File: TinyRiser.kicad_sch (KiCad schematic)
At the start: 25 parts, among them J2 Bus_PCI_Express_x16, J3 Bus_M.2_Socket_M, J5 Conn_02x04_Odd_Even, M1 Fan_4pin

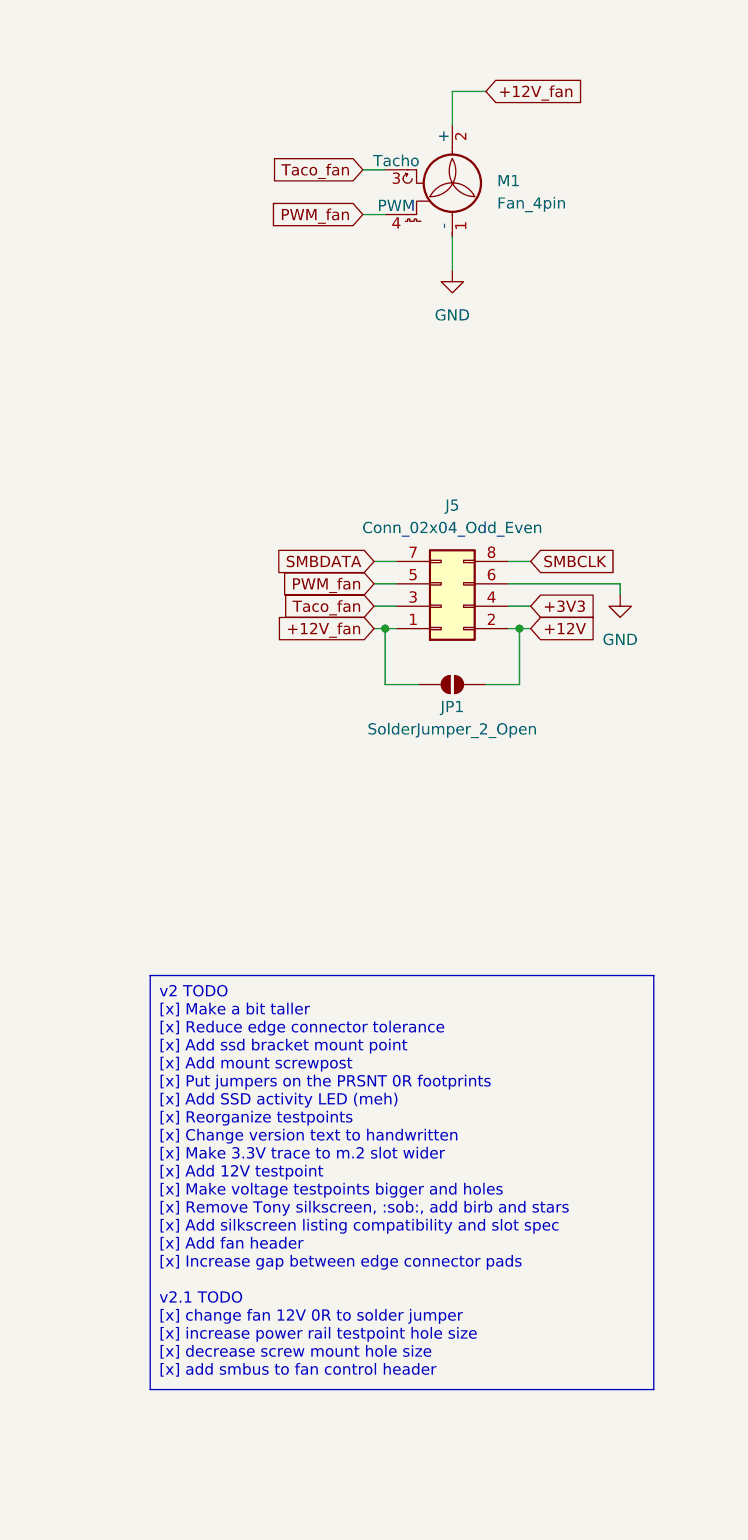
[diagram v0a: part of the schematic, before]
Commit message: Added JLC Assembly files and complete part list
Files exported using JLCPCB Tools 2026.04.03, not tested, please verify order on checkout.

Also updated PCB file from KiCad 8 to KiCad 9
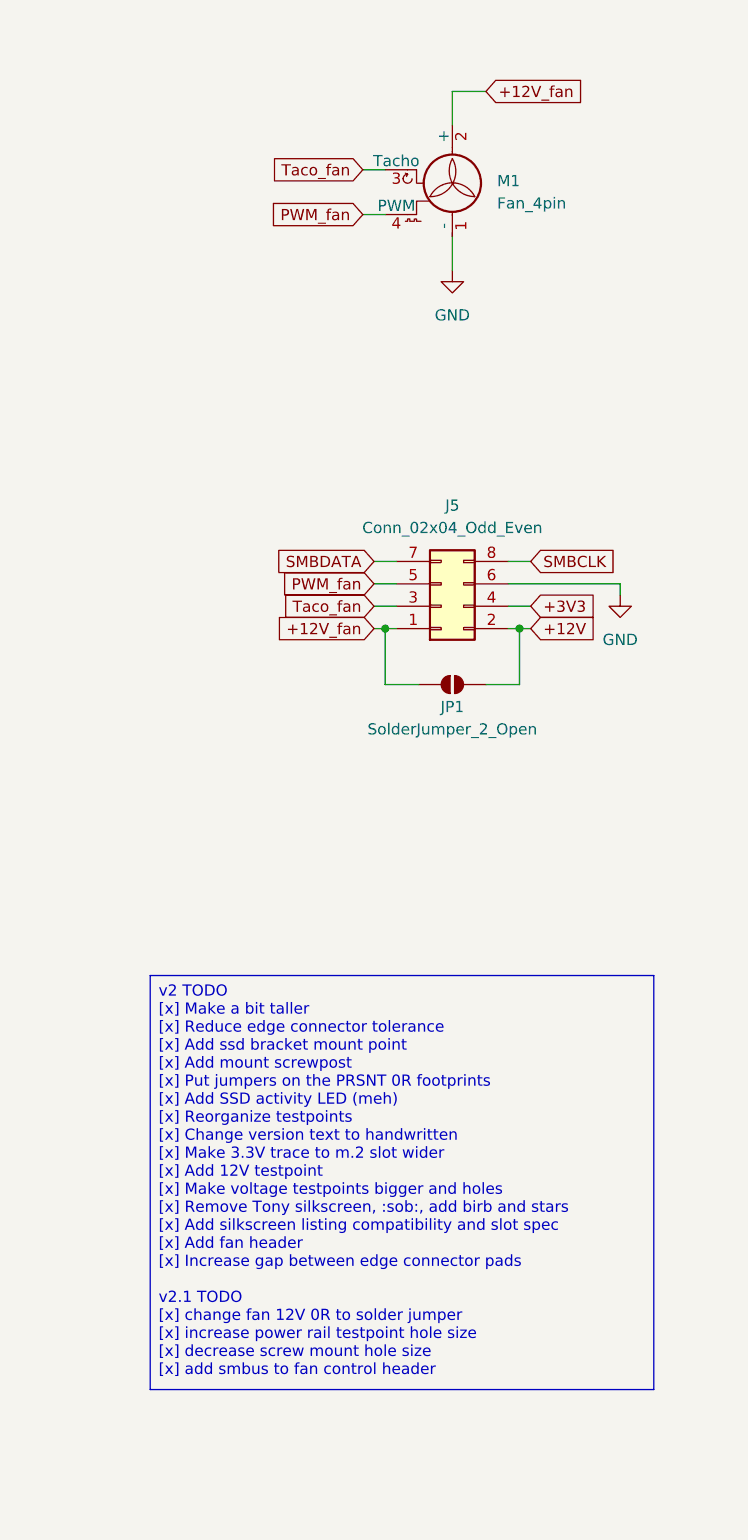
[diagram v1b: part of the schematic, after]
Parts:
- H1: LCSC Part (none) -> C5301786
- J1, J5, M1, R3, R4, R5, R6, TP1, TP2, TP3, TP4, TP5, TP6, TP7, TP8, TP9: now left out of the parts list
- J2: LCSC Part (none) -> C404116
- J3: LCSC Part (none) -> C41430861
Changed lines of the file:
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@@
 (kicad_sch
-	(version 20231120)
+	(version 20250114)
 	(generator "eeschema")
-	(generator_version "8.0")
+	(generator_version "9.0")
 	(paper "A3")
 	(title_block
@@
 		(comment 4 "nya")
 	)
+	(rectangle
+		(start 186.69 255.27)
+		(end 223.52 269.24)
+		(stroke
+			(width 0)
+			(type default)
+		)
+		(fill
+			(type none)
+		)
+	)
+	(text "Not a typo, that's how it's\nspelled on Lenovo's schematic"
+		(exclude_from_sim no)
+		(at 191.77 267.97 0)
+		(effects
+			(font
+				(size 1.27 1.27)
+			)
+			(justify left bottom)
+		)
+	)
+	(text "Note: CLKREQ# needs to be connected to GND to activate the clock signal.\nIf you're replacing the PCIe slot with an open-ended one,\nmake sure to account for longer cards where the presence pin is outside the slot.\nMaybe just hard-wire CLKREQ# to GND"
+		(exclude_from_sim no)
+		(at 237.744 22.606 0)
+		(effects
+			(font
+				(size 1.27 1.27)
+			)
+			(justify left)
+		)
+	)
+	(text_box "v2 TODO\n[x] Make a bit taller\n[x] Reduce edge connector tolerance\n[x] Add ssd bracket mount point\n[x] Add mount screwpost\n[x] Put jumpers on the PRSNT 0R footprints\n[x] Add SSD activity LED (meh)\n[x] Reorganize testpoints\n[x] Change version text to handwritten\n[x] Make 3.3V trace to m.2 slot wider\n[x] Add 12V testpoint\n[x] Make voltage testpoints bigger and holes\n[x] Remove Tony silkscreen, :sob:, add birb and stars\n[x] Add silkscreen listing compatibility and slot spec\n[x] Add fan header\n[x] Increase gap between edge connector pads\n\nv2.1 TODO\n[x] change fan 12V 0R to solder jumper\n[x] increase power rail testpoint hole size\n[x] decrease screw mount hole size\n[x] add smbus to fan control header"
+		(exclude_from_sim no)
+		(at 345.44 189.23 0)
+		(size 57.15 46.99)
+		(margins 0.9525 0.9525 0.9525 0.9525)
+		(stroke
+			(width 0)
+			(type default)
+		)
+		(fill
+			(type none)
+		)
+		(effects
+			(font
+				(size 1.27 1.27)
+			)
+			(justify left top)
+		)
+	)
 	(junction
 		(at 72.39 204.47)
@@
 		)
 	)
-	(rectangle
-		(start 186.69 255.27)
-		(end 223.52 269.24)
-		(stroke
-			(width 0)
-			(type default)
-		)
-		(fill
-			(type none)
-		)
-	)
-	(text_box "v2 TODO\n[x] Make a bit taller\n[x] Reduce edge connector tolerance\n[x] Add ssd bracket mount point\n[x] Add mount screwpost\n[x] Put jumpers on the PRSNT 0R footprints\n[x] Add SSD activity LED (meh)\n[x] Reorganize testpoints\n[x] Change version text to handwritten\n[x] Make 3.3V trace to m.2 slot wider\n[x] Add 12V testpoint\n[x] Make voltage testpoints bigger and holes\n[x] Remove Tony silkscreen, :sob:, add birb and stars\n[x] Add silkscreen listing compatibility and slot spec\n[x] Add fan header\n[x] Increase gap between edge connector pads\n\nv2.1 TODO\n[x] change fan 12V 0R to solder jumper\n[x] increase power rail testpoint hole size\n[x] decrease screw mount hole size\n[x] add smbus to fan control header"
-		(exclude_from_sim no)
-		(at 345.44 189.23 0)
-		(size 57.15 46.99)
-		(stroke
-			(width 0)
-			(type default)
-		)
-		(fill
-			(type none)
-		)
-		(effects
-			(font
-				(size 1.27 1.27)
-			)
-			(justify left top)
-		)
-	)
-	(text "Not a typo, that's how it's\nspelled on Lenovo's schematic"
-		(exclude_from_sim no)
-		(at 191.77 267.97 0)
-		(effects
-			(font
-				(size 1.27 1.27)
-			)
-			(justify left bottom)
-		)
-	)
-	(text "Note: CLKREQ# needs to be connected to GND to activate the clock signal.\nIf you're replacing the PCIe slot with an open-ended one,\nmake sure to account for longer cards where the presence pin is outside the slot.\nMaybe just hard-wire CLKREQ# to GND"
-		(exclude_from_sim no)
-		(at 237.744 22.606 0)
-		(effects
-			(font
-				(size 1.27 1.27)
-			)
-			(justify left)
-		)
-	)
 	(global_label "PCIe_PCH_Rx1-"
 		(shape input)
@@
 		(unit 1)
 		(exclude_from_sim no)
-		(in_bom yes)
+		(in_bom no)
 		(on_board yes)
 		(dnp no)
@@
 		(unit 1)
 		(exclude_from_sim no)
-		(in_bom yes)
+		(in_bom no)
 		(on_board yes)
 		(dnp no)
@@
 		(unit 1)
 		(exclude_from_sim no)
-		(in_bom yes)
+		(in_bom no)
 		(on_board yes)
 		(dnp no)
@@
 		(unit 1)
 		(exclude_from_sim no)
-		(in_bom yes)
+		(in_bom no)
 		(on_board yes)
 		(dnp no)
@@
 		(unit 1)
 		(exclude_from_sim no)
-		(in_bom yes)
+		(in_bom no)
 		(on_board yes)
 		(dnp no)
@@
 		(unit 1)
 		(exclude_from_sim no)
-		(in_bom yes)
+		(in_bom no)
 		(on_board yes)
 		(dnp no)
@@
 		(unit 1)
 		(exclude_from_sim no)
-		(in_bom yes)
+		(in_bom no)
 		(on_board yes)
 		(dnp no)
@@
 		(unit 1)
 		(exclude_from_sim no)
-		(in_bom yes)
+		(in_bom no)
 		(on_board yes)
 		(dnp no)
@@
 			)
 		)
+		(property "LCSC Part" "C5301786"
+			(at 372.11 64.77 0)
+			(effects
+				(font
+					(size 1.27 1.27)
+				)
+				(hide yes)
+			)
+		)
 		(pin "1"
 		)
@@
 			)
 		)
+		(property "LCSC Part" "C404116"
+			(at 208.28 74.93 90)
+			(effects
+				(font
+					(size 1.27 1.27)
+				)
+				(hide yes)
+			)
+		)
 		(pin "A1"
 		)
@@
 		(unit 1)
 		(exclude_from_sim no)
-		(in_bom yes)
+		(in_bom no)
 		(on_board yes)
 		(dnp no)
@@
 		(unit 1)
 		(exclude_from_sim no)
-		(in_bom yes)
+		(in_bom no)
 		(on_board yes)
 		(dnp no)
@@
 		(unit 1)
 		(exclude_from_sim no)
-		(in_bom yes)
+		(in_bom no)
 		(on_board yes)
 		(dnp no)
@@
 			)
 		)
+		(property "LCSC Part" "C41430861"
+			(at 59.69 74.93 0)
+			(effects
+				(font
+					(size 1.27 1.27)
+				)
+				(hide yes)
+			)
+		)
 		(pin "1"
 		)
@@
 		(unit 1)
 		(exclude_from_sim no)
-		(in_bom yes)
+		(in_bom no)
 		(on_board yes)
 		(dnp no)
@@
 		(unit 1)
 		(exclude_from_sim no)
-		(in_bom yes)
+		(in_bom no)
 		(on_board yes)
 		(dnp no)
@@
 		(unit 1)
 		(exclude_from_sim no)
-		(in_bom yes)
+		(in_bom no)
 		(on_board yes)
 		(dnp no)
@@
 		(unit 1)
 		(exclude_from_sim no)
-		(in_bom yes)
+		(in_bom no)
 		(on_board yes)
 		(dnp no)
@@
 		(unit 1)
 		(exclude_from_sim no)
-		(in_bom yes)
+		(in_bom no)
 		(on_board yes)
 		(dnp no)
@@
 		)
 	)
+	(embedded_fonts no)
 )
